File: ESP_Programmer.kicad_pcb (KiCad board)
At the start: 2 copper layers, 42.2 x 28.7 mm, 26 parts, among them J1 USB_B_Micro, J2 Conn_01x04_Female, J3 FTDI_Header, J4 ESP_PROG, Q1 MBT3904DW1T1G, U1 FT232RL-REEL

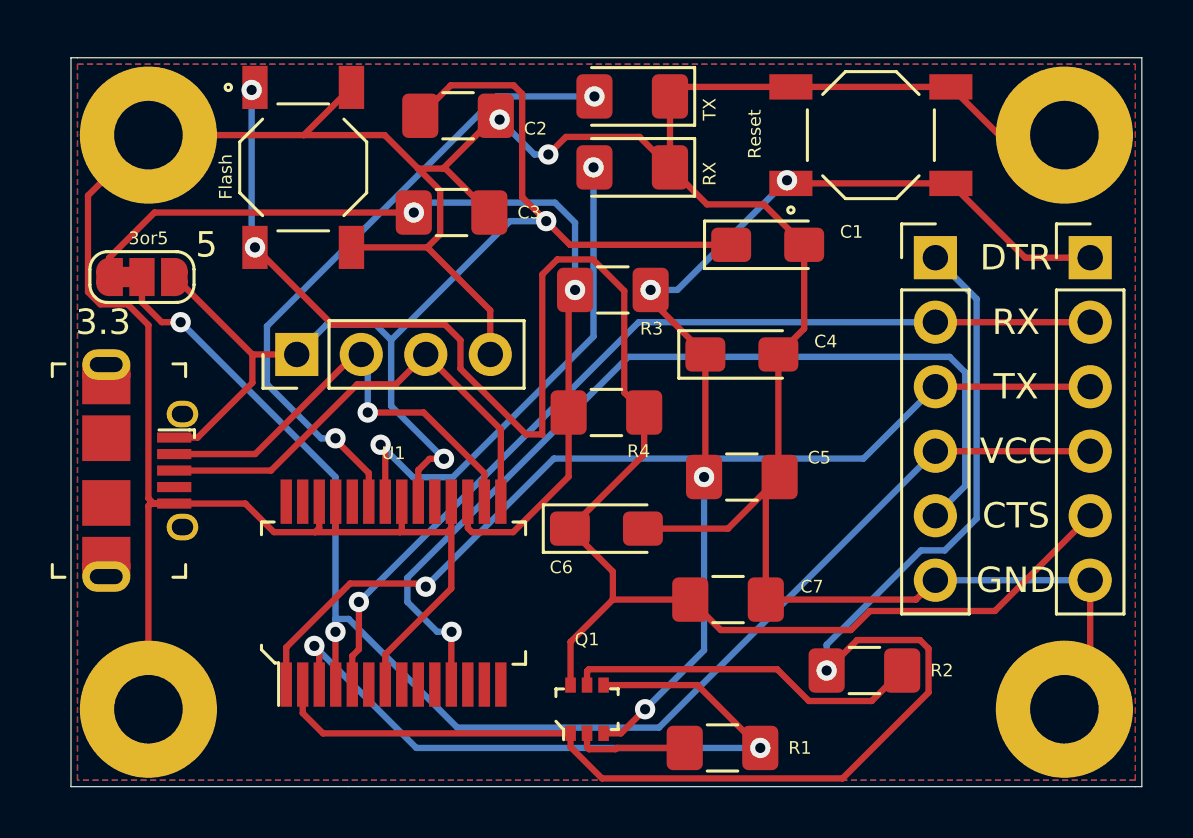
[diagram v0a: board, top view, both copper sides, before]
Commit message: V2 led's and notes about C6 & C7
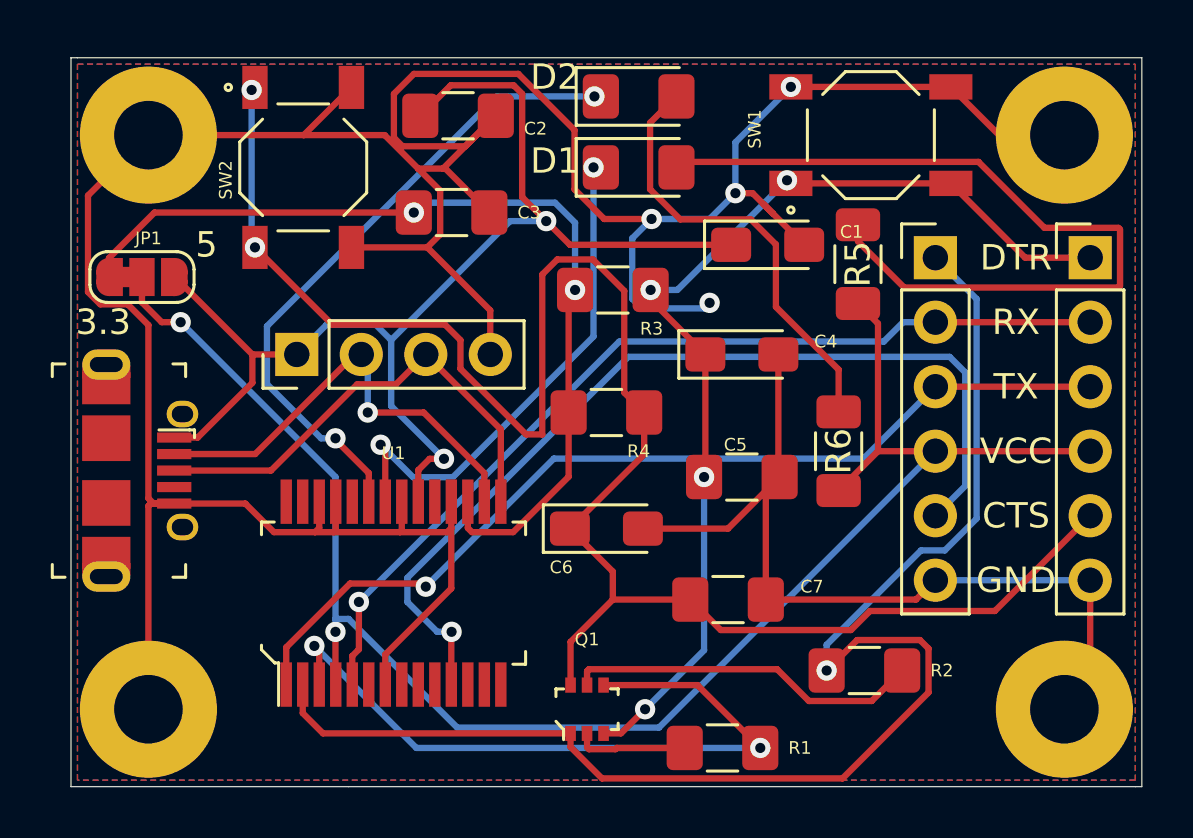
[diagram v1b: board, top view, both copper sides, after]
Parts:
- removed RX, TX: LED, LED_SMD:LED_1206_3216Metric_Pad1.42x1.75mm_HandSolder
- added D1: LED, LED_SMD:LED_1206_3216Metric_Pad1.42x1.75mm_HandSolder, F.Cu at (207.0, 92.5)
- added D2: LED, LED_SMD:LED_1206_3216Metric_Pad1.42x1.75mm_HandSolder, F.Cu at (207.0, 89.7)
- added R5: 270, Resistor_SMD:R_1206_3216Metric_Pad1.30x1.75mm_HandSolder, F.Cu at (215.6, 96.3)
- added R6: 270, Resistor_SMD:R_1206_3216Metric_Pad1.30x1.75mm_HandSolder, F.Cu at (214.9, 103.6)
- renumbered 3or5 to JP1, Reset to SW1, Flash to SW2
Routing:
- net Net-(D1-Pad2): track 0.00 -> 32.6 mm
- net Net-(D2-Pad2): track 0.00 -> 17.6 mm
- net GND: track 155.6 -> 168.7 mm, vias 2 -> 4
- net PWR_IO: track 55.6 -> 66.2 mm
